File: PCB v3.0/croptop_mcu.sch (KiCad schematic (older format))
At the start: 81 parts, among them J1 TSM-106-01-L-SV, J2 0473460001, J3 87583-2010BLF, J4 NREC004SABC-M30RC, Q1 BSS138, Q2 BSS84, SW1 SW_Push, U1 PIC32MX795F512L, U2 REG71055DDC, U3 AP22802AW5, U5 TPS62131RGT, U6 TPS70950DBV, U7 TPD4E1U06DBV, U8 TPD4E1U06DBV, Y1 ABLS-8.000MHZ-B4-T, Y3 ABS07-32.768KHZ-1-T

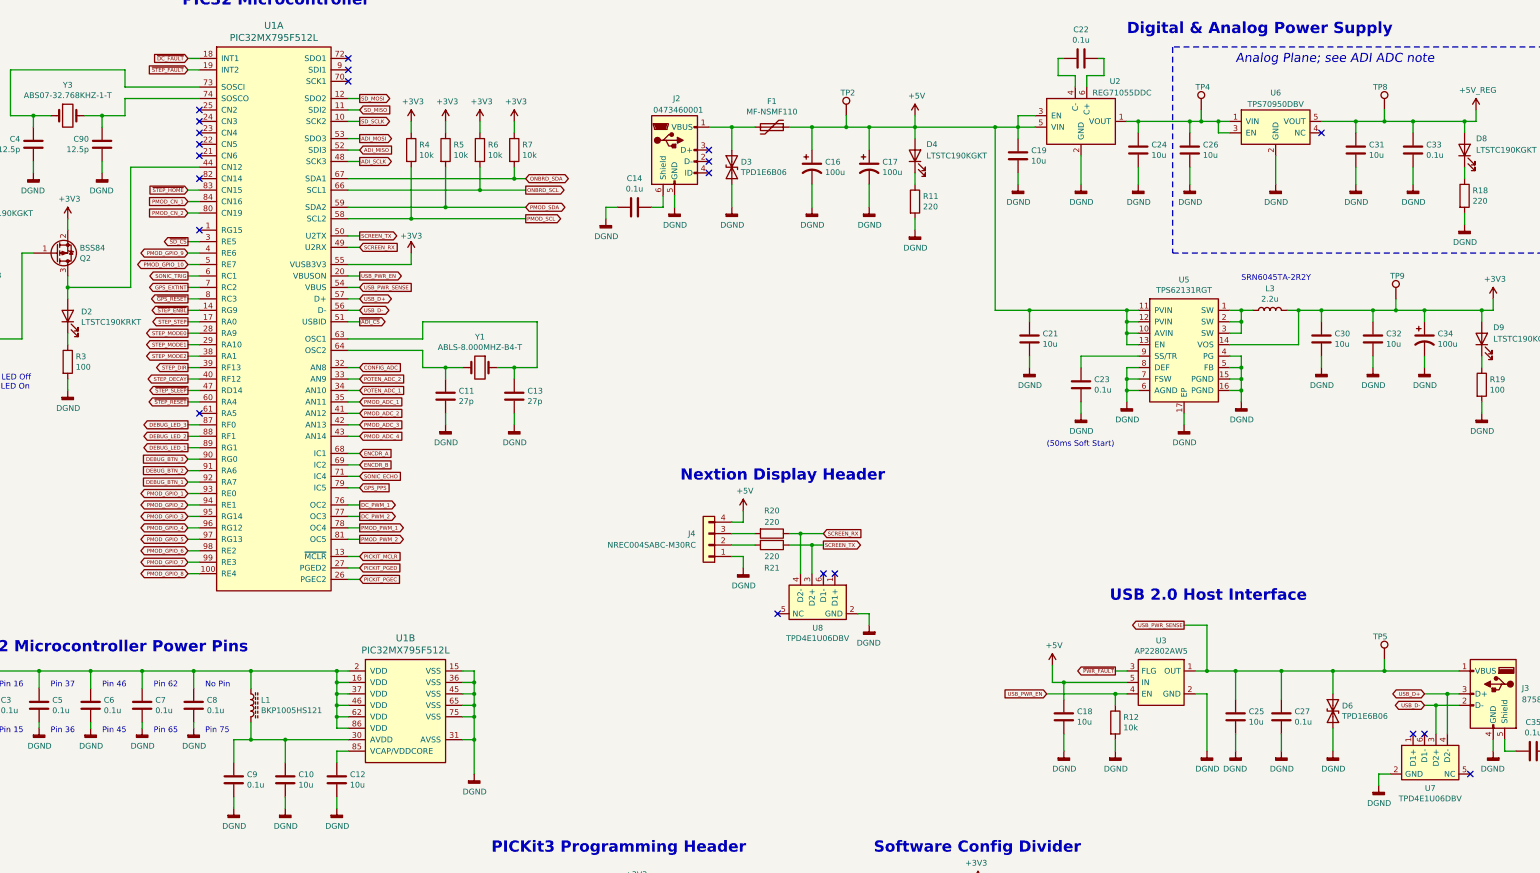
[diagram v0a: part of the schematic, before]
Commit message: Updated PCB dimensions for Nextion screen, deleted old files
- Updated PCB v3.0 to use the Nextion screen mounting and connectors
- Deleted old I2CDriver files from /Software/
- Deleted unused /Software/Readme
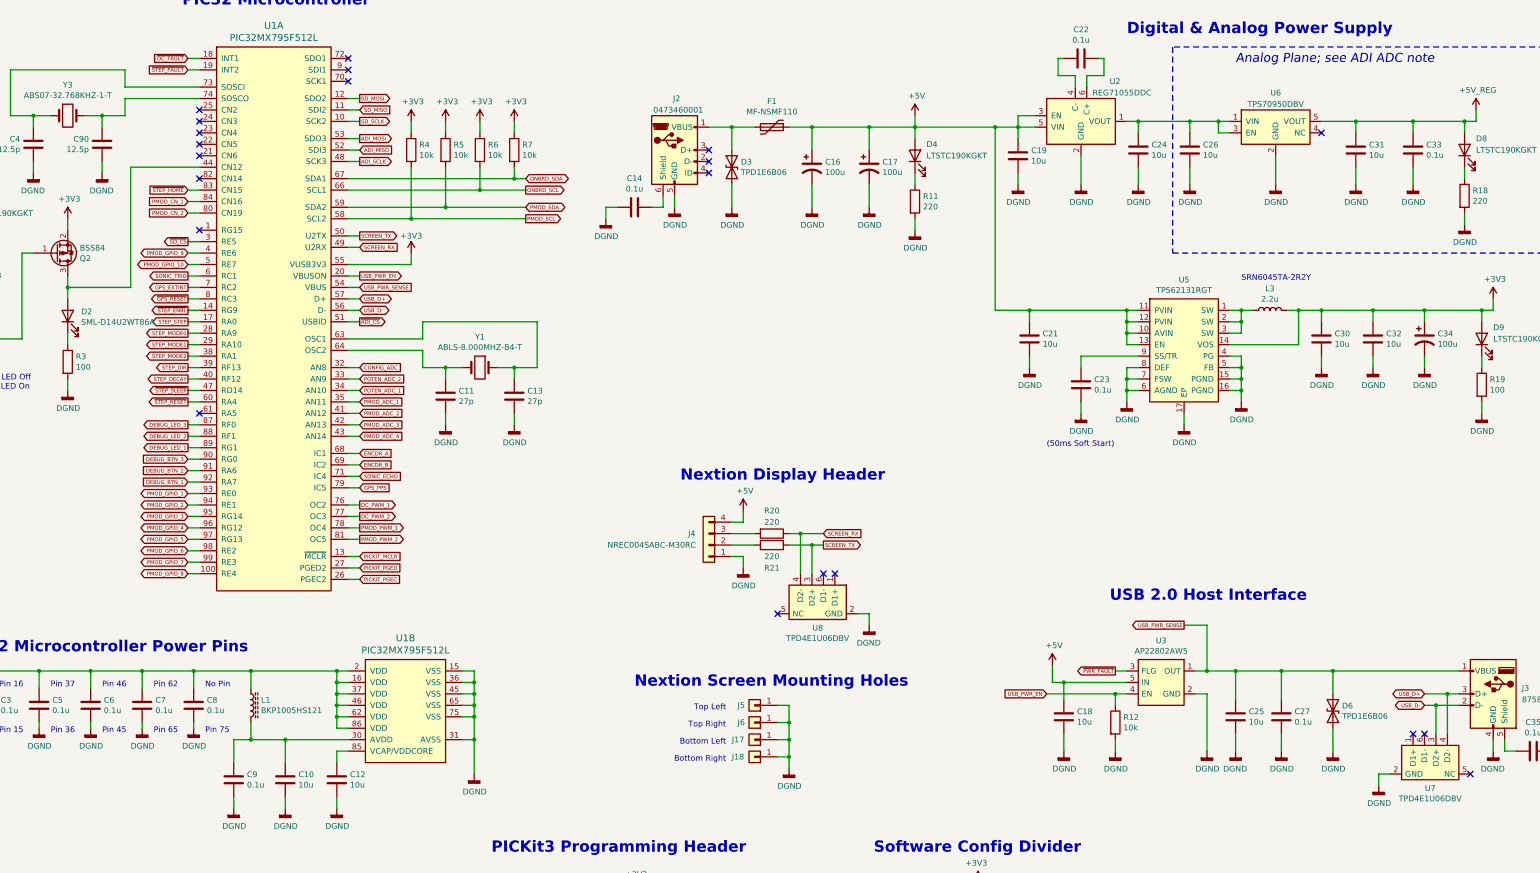
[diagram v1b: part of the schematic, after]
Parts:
- removed TP2, TP4, TP5, TP8, TP9: TestPoint, TestPoint:TestPoint_Pad_D1.0mm, symbol Connector:TestPoint
- added J17, J18, J5, J6: Conn_01x01, MountingHole:MountingHole_3.2mm_M3_Pad_Via, symbol Connector_Generic:Conn_01x01
- D2: value LTSTC190KRKT -> SML-D14U2WT86A; MPN LTST-C190KRKT -> SML-D14U2WT86A
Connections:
- net DGND: now also J17.1 (Pin_1), J18.1 (Pin_1), J5.1 (Pin_1), J6.1 (Pin_1)
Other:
- note added: "Bottom Left"
- note added: "Bottom Right\n"
- note added: "Nextion Screen Mounting Holes\n"
- note added: "Top Left"
- note added: "Top Right"
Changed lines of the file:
@@
 $EndComp
 $Comp
-L Connector:TestPoint TP?
-U 1 1 5CB340DF
-P 9450 1800
-AR Path="/64809F0C/5CB340DF" Ref="TP?"  Part="1"
-AR Path="/64807BBC/5CB340DF" Ref="TP2"  Part="1"
-F 0 "TP2" H 9400 2000 50  0000 L CNN
-F 1 "TestPoint" H 9508 1829 50  0001 L CNN
-F 2 "TestPoint:TestPoint_Pad_D1.0mm" H 9650 1800 50  0001 C CNN
-F 3 "" H 9650 1800 50  0001 C CNN
-	1    9450 1800
-	1    0    0    -1
-$EndComp
-$Comp
-L Connector:TestPoint TP?
-U 1 1 5CB3411D
-P 14250 3400
-AR Path="/64809F0C/5CB3411D" Ref="TP?"  Part="1"
-AR Path="/64807BBC/5CB3411D" Ref="TP9"  Part="1"
-F 0 "TP9" H 14200 3600 50  0000 L CNN
-F 1 "TestPoint" H 14308 3429 50  0001 L CNN
-F 2 "TestPoint:TestPoint_Pad_D1.0mm" H 14450 3400 50  0001 C CNN
-F 3 "" H 14450 3400 50  0001 C CNN
-	1    14250 3400
-	1    0    0    -1
-$EndComp
-Wire Wire Line
-	14250 3400 14250 3500
-$Comp
 L Device:LED D?
 U 1 1 5CB34125
@@
 	15000 3500 15000 3600
 Wire Wire Line
-	9450 1800 9450 1900
-Wire Wire Line
-	13900 1850 14150 1850
-Wire Wire Line
 	14950 1850 14950 1750
 Connection ~ 13900 1850
 $Comp
-L Connector:TestPoint TP?
-U 1 1 5CB34141
-P 14150 1750
-AR Path="/64809F0C/5CB34141" Ref="TP?"  Part="1"
-AR Path="/64807BBC/5CB34141" Ref="TP8"  Part="1"
-F 0 "TP8" H 14050 1950 50  0000 L CNN
-F 1 "TestPoint" H 14208 1779 50  0001 L CNN
-F 2 "TestPoint:TestPoint_Pad_D1.0mm" H 14350 1750 50  0001 C CNN
-F 3 "" H 14350 1750 50  0001 C CNN
-	1    14150 1750
-	1    0    0    -1
-$EndComp
-Wire Wire Line
-	14150 1750 14150 1850
-$Comp
-L Connector:TestPoint TP?
-U 1 1 5CB34149
-P 12550 1750
-AR Path="/64809F0C/5CB34149" Ref="TP?"  Part="1"
-AR Path="/64807BBC/5CB34149" Ref="TP4"  Part="1"
-F 0 "TP4" H 12500 1950 50  0000 L CNN
-F 1 "TestPoint" H 12608 1779 50  0001 L CNN
-F 2 "TestPoint:TestPoint_Pad_D1.0mm" H 12750 1750 50  0001 C CNN
-F 3 "" H 12750 1750 50  0001 C CNN
-	1    12550 1750
-	1    0    0    -1
-$EndComp
-$Comp
 L Device:LED D?
 U 1 1 5CB34158
@@
 Wire Wire Line
 	10050 1800 10050 1900
-Connection ~ 14150 1850
 Wire Wire Line
 	9150 2400 9150 2600
@@
 $EndComp
 Wire Wire Line
-	12450 1850 12550 1850
-Wire Wire Line
 	13200 2150 13200 2400
 $Comp
@@
 	14050 3600 14050 3500
 Connection ~ 14050 3500
-Wire Wire Line
-	14050 3500 14250 3500
-Connection ~ 14250 3500
-Wire Wire Line
-	14250 3500 14500 3500
 $Comp
 L Device:C C?
@@
 	14400 2250 14400 2400
 Wire Wire Line
-	14150 1850 14400 1850
-Wire Wire Line
 	14400 1850 14400 1950
 Connection ~ 14400 1850
@@
 	11350 7200 11350 7350
 $Comp
-L Connector:TestPoint TP?
-U 1 1 5CB345D6
-P 14150 6550
-AR Path="/64809F0C/5CB345D6" Ref="TP?"  Part="1"
-AR Path="/66A12230/5CB345D6" Ref="TP?"  Part="1"
-AR Path="/64807BBC/5CB345D6" Ref="TP5"  Part="1"
-F 0 "TP5" H 14050 6750 50  0000 L CNN
-F 1 "TestPoint" H 14208 6579 50  0001 L CNN
-F 2 "TestPoint:TestPoint_Pad_D1.0mm" H 14350 6550 50  0001 C CNN
-F 3 "" H 14350 6550 50  0001 C CNN
-	1    14150 6550
-	1    0    0    -1
-$EndComp
-Wire Wire Line
-	14150 6550 14150 6650
-$Comp
 L CropTop:AP22802AW5 U3
 U 1 1 5CB345DE
@@
 Connection ~ 11800 6850
 Wire Wire Line
-	13700 6650 14150 6650
-Wire Wire Line
 	14700 6850 14700 7200
 Wire Wire Line
@@
 Wire Wire Line
 	12000 1850 12450 1850
-Connection ~ 12550 1850
-Wire Wire Line
-	12550 1850 12700 1850
-Wire Wire Line
-	12550 1750 12550 1850
 $Comp
 L CropTop:DGND #PWR077
@@
 Wire Wire Line
 	1000 3650 1000 3750
-Connection ~ 14150 6650
-Wire Wire Line
-	14150 6650 14800 6650
 Wire Wire Line
 	12600 6650 12500 6650
@@
 AR Path="/64807BBC/6051C257" Ref="D2"  Part="1"
 F 0 "D2" V 2688 3433 50  0000 R CNN
-F 1 "LTSTC190KRKT" V 2597 3433 50  0000 R CNN
+F 1 "SML-D14U2WT86A" V 2597 3433 50  0000 R CNN
 F 2 "LED_SMD:LED_0603_1608Metric" H 2650 3550 50  0001 C CNN
 F 3 "" H 2650 3550 50  0001 C CNN
-F 4 "LTST-C190KRKT" V 2650 3550 50  0001 C CNN "MPN"
+F 4 "SML-D14U2WT86A" V 2650 3550 50  0001 C CNN "MPN"
 	1    2650 3550
 	0    -1   -1   0
@@
 Connection ~ 9150 1900
 Wire Wire Line
-	9150 1900 9450 1900
-Connection ~ 9450 1900
-Wire Wire Line
-	9450 1900 9650 1900
-Wire Wire Line
 	10050 1900 10750 1900
 Wire Wire Line
@@
 Wire Wire Line
 	3700 3100 3800 3100
+Wire Wire Line
+	12450 1850 12700 1850
+Wire Wire Line
+	14050 3500 14500 3500
+Wire Wire Line
+	13900 1850 14400 1850
+Wire Wire Line
+	9150 1900 9650 1900
+Wire Wire Line
+	13700 6650 14800 6650
+$Comp
+L Connector_Generic:Conn_01x01 J5
+U 1 1 5EC22E4D
+P 8650 6950
+F 0 "J5" H 8800 6950 50  0000 R CNN
+F 1 "Conn_01x01" V 8523 6862 50  0001 R CNN
+F 2 "MountingHole:MountingHole_3.2mm_M3_Pad_Via" H 8650 6950 50  0001 C CNN
+F 3 "~" H 8650 6950 50  0001 C CNN
+	1    8650 6950
+	-1   0    0    1
+$EndComp
+Text Notes 8400 7000 2    50   ~ 0
+Top Left
+$Comp
+L Connector_Generic:Conn_01x01 J6
+U 1 1 5EC2A03A
+P 8650 7100
+F 0 "J6" H 8800 7100 50  0000 R CNN
+F 1 "Conn_01x01" V 8523 7012 50  0001 R CNN
+F 2 "MountingHole:MountingHole_3.2mm_M3_Pad_Via" H 8650 7100 50  0001 C CNN
+F 3 "~" H 8650 7100 50  0001 C CNN
+	1    8650 7100
+	-1   0    0    1
+$EndComp
+Text Notes 8400 7150 2    50   ~ 0
+Top Right
+$Comp
+L Connector_Generic:Conn_01x01 J17
+U 1 1 5EC55204
+P 8650 7250
+F 0 "J17" H 8850 7250 50  0000 R CNN
+F 1 "Conn_01x01" V 8523 7162 50  0001 R CNN
+F 2 "MountingHole:MountingHole_3.2mm_M3_Pad_Via" H 8650 7250 50  0001 C CNN
+F 3 "~" H 8650 7250 50  0001 C CNN
+	1    8650 7250
+	-1   0    0    1
+$EndComp
+Text Notes 8400 7300 2    50   ~ 0
+Bottom Left
+$Comp
+L Connector_Generic:Conn_01x01 J18
+U 1 1 5EC804EC
+P 8650 7400
+F 0 "J18" H 8850 7400 50  0000 R CNN
+F 1 "Conn_01x01" V 8523 7312 50  0001 R CNN
+F 2 "MountingHole:MountingHole_3.2mm_M3_Pad_Via" H 8650 7400 50  0001 C CNN
+F 3 "~" H 8650 7400 50  0001 C CNN
+	1    8650 7400
+	-1   0    0    1
+$EndComp
+Text Notes 8400 7450 2    50   ~ 0
+Bottom Right\n
+$Comp
+L CropTop:DGND #PWR043
+U 1 1 5ED06B33
+P 8950 7500
+AR Path="/64807BBC/5ED06B33" Ref="#PWR043"  Part="1"
+AR Path="/64809F0C/5ED06B33" Ref="#PWR?"  Part="1"
+F 0 "#PWR043" H 8950 7250 50  0001 C CNN
+F 1 "DGND" H 8954 7345 50  0000 C CNN
+F 2 "" H 8950 7500 50  0001 C CNN
+F 3 "" H 8950 7500 50  0001 C CNN
+	1    8950 7500
+	1    0    0    -1
+$EndComp
+Wire Wire Line
+	8950 7500 8950 7400
+Wire Wire Line
+	8950 7400 8850 7400
+Wire Wire Line
+	8850 7250 8950 7250
+Wire Wire Line
+	8950 7250 8950 7400
+Connection ~ 8950 7400
+Wire Wire Line
+	8850 7100 8950 7100
+Wire Wire Line
+	8950 7100 8950 7250
+Connection ~ 8950 7250
+Wire Wire Line
+	8850 6950 8950 6950
+Wire Wire Line
+	8950 6950 8950 7100
+Connection ~ 8950 7100
+Text Notes 7600 6800 0    98   ~ 20
+Nextion Screen Mounting Holes\n
 $EndSCHEMATC
